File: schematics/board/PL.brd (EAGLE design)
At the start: 89 x 89 mm, 39 parts, among them IC2 STM32F103C8T, Q5 8MHz

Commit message: Папка с платами
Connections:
- net 5V: now also BSK4.3; no longer BSK4.8
- net BUS+: now also BSK4.4; no longer BSK4.7
- net I2CINT: now also BSK4.6; no longer BSK4.3
- net SCLTM: now also BSK4.8; no longer BSK4.5
- net SDATM: now also BSK4.7; no longer BSK4.4
- net TIME: now also BSK4.5; no longer BSK4.2
- net VDD: now also BSK4.2; no longer BSK4.6
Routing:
- net 5V: track 109.7 -> 122.4 mm
- net SDATM: track 38.2 -> 31.7 mm
- net I2CINT: track 29.2 -> 24.5 mm
- net TIME: track 31.1 -> 27.0 mm
- net VDD: track 265.3 -> 267.5 mm
- net NRST: track 49.2 -> 47.8 mm
- net SCLTM: track 32.4 -> 31.8 mm, vias 2 -> 4

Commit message: Обновлен список плат, работа над платой ПН
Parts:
- removed BSK4: (no value), pinheadCS:1X08
- removed C005R: 32,768KHz, CanCubeSat:C005R
- removed C15, C48, C53, C54, C55: 100nF, rcl:C0603
- removed C16: 10µ, rcl:C1206
- removed C44, C45: 27pF, rcl:C0603
- removed C46, C47: 10pF, rcl:C0603
- removed IC2: STM32F103C8T, CanCubeSat:LQFP48
- removed ME-O2: ME-O2, CanCubeSat:ME-O2
- removed MICS-6814: MICS-6814, CanCubeSat:MICS-6814
- removed PB5, PWR: (no value), led:CHIPLED_0603
- removed Q5: 8MHz, 9C-8.000MEEJ-T:XTAL_9C-8.000MEEJ-T
- removed R101, R102: 5k1, resistor:R0603
- removed R64, R79: 10k, resistor:R0603
- removed R78: 1M, resistor:R0603
- removed R81, R82: 2k, resistor:R0603
- removed USB-C: USB-C, CanCubeSat:USB-C
- added 2N6517, BC546: DS1820, CanCubeSat:TO92/TO226
- added BSK1: (no value), pinheadCS:2X05
- added C1, C18, C2, C20, C3, C6: 100nF, rcl:C0603
- added C10: 10nF, rcl:C0603
- added C13, C9: 2,2µ, rcl:C0603
- added C19: 10µ, rcl:C1206
- added C4, C5: 22nF, rcl:C1210
- added C7: 100pF, rcl:C0603
- added C8: 1nF, rcl:C0603
- added COMPR, HEAT, TEMP, VALVE1, VALVE2: (no value), pinheadCS:1X02
- added D1, D2, D3, D4, D5: DIODE-MBR, CanCubeSat:SOD123
- added LED2, LED3: (no value), led:CHIPLED_0603
- added R10, R11, R12, R37, R38, R39, R40, R41, R42, R43, R44, R45: 10k, resistor:R0603
- added R13, R20, R24, R30, R34, R48: 0.05A, rcl:R1210
- added R14, R21, R22, R28, R32, R46, R49, R53, R55: 1M, resistor:R0603
- added R15, R16: 2k, resistor:R0603
- added R17, R18: 5k1, resistor:R0603
- added R19, R23, R29, R31, R33, R47, R50, R54, R56: 100R, resistor:R0603
- added R35: 100k, resistor:R0603
- added R36: 3k3, resistor:R0603
- added R51: 124k, resistor:R0603
- added R52: 22k, resistor:R0603
- added U$1: MS5611, CanCubeSat:MS5611
- added U$10, U$11, U$12, U$13: BA159, CanCubeSat:BA159
- added U$14: ECAP, CanCubeSat:ECAP1MK
- added U$15: DOSIM, CanCubeSat:DOSIM
- added U$16, U$21: FFC-CONNECT68611, CanCubeSat:68611
- added U$17: 33mH, CanCubeSat:RCH114NP
- added U$18, U$19, U$20, U$22, U$23, U$3, U$4, U$5, U$7, U$8: SI2302CDS, CanCubeSat:SOT23-3
- added U$2: Q24, CanCubeSat:Q24
- added U$9: 100µ, CanCubeSat:ECAP100-CMD
- added U1: STM32F405RGT6, STM32F405RGT6:QFP50P1200X1200X160-64N
- added U2: LMC555CMX/NOPB, LMC555CMX_NOPB:SOIC127P599X175-8N
- added VR1: 3362H-1-502LF, CanCubeSat:TRIM_3362H-1-502LF
- R1: value 10k -> 0.5A; device resistor:R0603 -> rcl:R1210
- R2: value 10k -> 1k
- R25: value 5k1 -> 1M
- R26: value 5k1 -> 100R
- R27: value 10k -> 0.05A; device resistor:R0603 -> rcl:R1210
- R3: value 10k -> 4k7
- R4: value 10k -> 22k
- R5, R6, R7, R8, R9: value 10k -> 1M
- moved R1 310.3 mm to (3.00, -247.0), turned to 0 degrees
- moved R26 226.4 mm to (1.50, -193.5), turned to 0 degrees
- moved R25 224.3 mm to (7.50, -193.5), turned to 0 degrees
- moved R27 218.6 mm to (3.00, -187.0), turned to 0 degrees
- moved R3 191.3 mm to (-126.0, 107.0), turned to 0 degrees
- moved R2 123.6 mm to (-57.0, 88.0), turned to 0 degrees
- moved BME280 110.5 mm to (-17.5, -18.5)
- moved R4 55.6 mm to (12.5, 40.0), turned to 0 degrees
- moved R9 54.2 mm to (12.5, 52.5), turned to 0 degrees
- moved R5 51.1 mm to (12.5, 42.5), turned to 0 degrees
- moved R8 50.1 mm to (12.5, 50.0), turned to 0 degrees
- moved R6 46.7 mm to (12.5, 45.0), turned to 0 degrees
- moved R7 46.1 mm to (12.5, 47.5), turned to 0 degrees
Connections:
- removed net I2CINT: BSK4.6, IC2.43
- removed net N$133: C44.1, IC2.6, Q5.1, R78.1
- removed net N$145: C45.1, IC2.5, Q5.2, R78.2
- removed net N$148: C005R.P$2, C47.1, IC2.4
- removed net N$152: C005R.P$1, C46.1, IC2.3
- removed net N$159: PWR.C, R82.2
- removed net N$161: IC2.41, R81.1
- removed net RX-C: IC2.31, USB-C.RX0
- removed net SCLTM: BSK4.8, IC2.45, R25.2
- removed net SDATM: BSK4.7, IC2.46, R26.2
- removed net SENS_CO: IC2.12, MICS-6814.P$5, R3.1
- removed net SENS_CTL_CO_1: IC2.19, R3.2, R6.1
- removed net SENS_CTL_CO_2: IC2.18, R6.2, R7.1
- removed net SENS_CTL_NH3_1: IC2.17, R2.2, R5.1
- removed net SENS_CTL_NH3_2: IC2.16, R5.2, R8.1
- removed net SENS_CTL_NO2_1: IC2.15, R1.2, R4.1
- removed net SENS_CTL_NO2_2: IC2.14, R4.2, R9.1
- removed net SENS_NH3: IC2.11, MICS-6814.P$4, R2.1
- removed net SENS_NO2: IC2.10, MICS-6814.P$3, R1.1
- removed net SENS_O2: IC2.13, ME-O2.P$1
- removed net TX-C: IC2.30, USB-C.TX0
- removed net VDD: BSK4.2, C15.1, C16.1, C48.1, C53.1, C54.1, C55.1, IC2.1, IC2.24, IC2.36, IC2.48, IC2.9, ME-O2.P$7, PB5.A, PWR.A, R101.1, R102.1, R25.1, R26.1, R27.1, R64.1, R7.2, R79.1, R8.2, R9.2, USB-C.3V3/BUS0, USB-C.3V3/BUS1
- new net 3V3: BSK1.3, C10.2, C18.2, C19.2, C2.2, C20.2, C3.2, C6.2, LED2.A, LED3.A, R10.2, R11.2, R12.2, R17.1, R18.1, R43.2, R44.2, R45.2, R52.2, U$2.P$4, U$21.P$1, U$21.P$2, U1.1, U1.13, U1.19, U1.32, U1.48, U1.64
- new net 4OXV: R26.1, U1.9
- new net BME280-EXT: R19.1, U1.35
- new net BME280-INT: R47.1, U1.34
- new net CO: R39.1, U$16.P$7, U1.16
- new net COMPR: R54.1, U1.57
- new net CTRL-CO-1: R39.2, R42.1, U1.27
- new net CTRL-CO-2: R42.2, R43.1, U1.26
- new net CTRL-NH3-1: R38.2, R41.1, U1.45
- new net CTRL-NH3-2: R41.2, R44.1, U1.44
- new net CTRL-NO2-1: R37.2, R40.1, U1.23
- new net CTRL-NO2-2: R40.2, R45.1, U1.22
- new net DOS-G: 2N6517.1, BC546.1, C1.1, C5.2, D1.A, R34.1, R35.2, U$10.P$1, U$14.P$2, U$9.P$1, U2.1
- new net DOSE: BC546.3, C7.2, R36.2
- new net DOSIM: R33.1, U1.10
- new net G-4OXV: R27.1, U$16.P$2
- new net G-BME: R48.1, U$16.P$14
- new net G-MICS: R24.1, U$16.P$6
- new net G-MS: R30.1, U$16.P$11
- new net GND-40XV: U$5.3
- new net GND-4OXV: R27.2
- new net GND-BME-EXT: R20.2, U$3.3
- new net GND-BME-INT: R48.2, U$18.3
- new net GND-COMPR: COMPR.2, U$22.3
- new net GND-DOSIM: R34.2, U$8.3
- new net GND-HEAT: HEAT.2, U$23.3
- new net GND-MICS: R24.2, U$4.3
- new net GND-MS-EXT: R13.2, U$19.3
- new net GND-MS-INT: R30.2, U$7.3
- new net GND-OUT: BSK1.5, BSK1.6, R1.2
- new net GND-VALVE: U$20.3, VALVE1.2, VALVE2.2
- new net HEAT: R56.1, U1.11
- new net MICS: R23.1, U1.8
- new net MS5611-EXT: R31.1, U1.41
- new net MS5611-INT: R29.1, U1.33
- new net N$10: R46.1, R47.2, U$18.1
- new net N$11: R22.1, R31.2, U$19.1
- new net N$12: R28.1, R29.2, U$7.1
- new net N$14: R32.1, R33.2, U$8.1
- new net N$15: C1.2, R2.1, U2.2, U2.6
- new net N$16: R2.2, VR1.2, VR1.3
- new net N$17: R3.2, U2.3, VR1.1
- new net N$18: 2N6517.2, R3.1
- new net N$19: 2N6517.3, C4.1, U$10.P$2, U$11.P$1, U$17.P$2
- new net N$2: R14.1, R19.2, U$3.1
- new net N$20: C5.1, U$11.P$2, U$12.P$1
- new net N$21: C4.2, U$12.P$2, U$13.P$1
- new net N$22: R4.2, R5.2, U$13.P$2, U$14.P$1
- new net N$23: D1.C, D2.A
- new net N$24: D2.C, D3.A
- new net N$25: D3.C, D4.A
- new net N$26: D4.C, D5.A
- new net N$27: D5.C, R4.1
- new net N$28: R5.1, R6.1
- new net N$29: C13.2, U1.47
- new net N$3: BME280.P$2, R20.1
- new net N$30: R6.2, R7.2
- new net N$31: R7.1, R8.1
- new net N$32: R8.2, R9.2
- new net N$33: R9.1, U$15.P$1
- new net N$34: BC546.2, C7.1, R35.1, U$15.P$2
- new net N$36: C9.2, U1.31
- new net N$37: LED2.C, R15.2
- new net N$38: R15.1, U1.53
- new net N$4: C8.2, U$2.P$3
- new net N$40: LED3.C, R16.2
- new net N$47: R53.1, R54.2, U$22.1
- new net N$48: R55.1, R56.2, U$23.1
- new net N$5: C8.1, U1.5
- new net N$6: R21.1, R23.2, U$4.1
- new net N$7: R49.1, R50.2, U$20.1
- new net N$8: R25.1, R26.2, U$5.1
- new net NH3: R38.1, U$16.P$8, U1.15
- new net NO2: R37.1, U$16.P$9, U1.14
- new net RX-O2: U$16.P$4, U1.43
- new net RX-S: U$21.P$5, U1.51
- new net SCL-TM: BSK1.7, U1.29
- new net SDA-TM: BSK1.8, U1.30
- new net TEMP: R51.2, R52.1, TEMP.1, U1.20
- new net TX-O2: U$16.P$3, U1.42
- new net TX-S: U$21.P$7, U1.52
- new net VALVE: R50.1, U1.61
- net 5V: now also BSK1.4, HEAT.1, R36.1, U$1.P$1, U$1.P$7, U$16.P$1, U$16.P$10, U$16.P$15, U$16.P$5, U$17.P$1, U$9.P$2, U2.4, U2.8, VALVE1.1, VALVE2.1; no longer BSK4.3, MICS-6814.P$1
- net BUS+: now also BSK1.2, COMPR.1; no longer BSK4.4
- net GND: now also C10.1, C13.1, C18.1, C19.1, C2.1, C20.1, C3.1, C6.1, C9.1, R1.1, R14.2, R16.1, R21.2, R22.2, R25.2, R28.2, R32.2, R46.2, R49.2, R51.1, R53.2, R55.2, TEMP.2, U$18.2, U$19.2, U$2.P$2, U$20.2, U$21.P$10, U$21.P$4, U$21.P$6, U$21.P$8, U$22.2, U$23.2, U$3.2, U$4.2, U$5.2, U$7.2, U$8.2, U1.12, U1.18, U1.28, U1.60, U1.63; no longer BME280.P$2, BSK4.1, C15.2, C16.2, C44.2, C45.2, C46.2, C47.2, C48.2, C53.2, C54.2, C55.2, IC2.20, IC2.23, IC2.35, IC2.44, IC2.47, IC2.8, ME-O2.P$4, MICS-6814.P$2, R82.1, USB-C.GND0, USB-C.GND1
- net N$1: now also R13.1, U$1.P$3, U$1.P$6; no longer PB5.C, R81.2
- net NRST: now also R10.1, U$21.P$3, U1.7; no longer IC2.7, R79.2, USB-C.NRST/EN
- net SCL: now also R17.2, U$1.P$5, U$16.P$12, U1.58; no longer IC2.21, R101.2
- net SDA: now also R18.2, U$1.P$4, U$16.P$13, U1.59; no longer IC2.22, R102.2
- net SWC: now also R12.1, U$21.P$11, U1.49; no longer IC2.37, R27.2, USB-C.SWC/TXD
- net SWD: now also R11.1, U$21.P$9, U1.46; no longer IC2.34, R64.2, USB-C.SWD/RXD
- net TIME: now also BSK1.9, U1.50; no longer BSK4.5, IC2.42
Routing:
- net VDD: track 267.5 -> 0.00 mm, vias 13 -> 0
- net 5V: track 122.4 -> 0.00 mm
- net NRST: track 47.8 -> 0.00 mm, vias 2 -> 0
- net GND: track 40.0 -> 0.00 mm, vias 3 -> 0
- net SENS_CO: track 36.7 -> 0.00 mm, vias 1 -> 0
- net SENS_NH3: track 36.7 -> 0.00 mm, vias 1 -> 0
- net SENS_NO2: track 34.2 -> 0.00 mm, vias 2 -> 0
- net TX-C: track 34.0 -> 0.00 mm, vias 2 -> 0
- net SDA: track 32.3 -> 0.00 mm, vias 1 -> 0
- net SCLTM: track 31.8 -> 0.00 mm, vias 4 -> 0
- net SDATM: track 31.7 -> 0.00 mm
- net SENS_O2: track 30.6 -> 0.00 mm, vias 4 -> 0
- net RX-C: track 29.7 -> 0.00 mm, vias 2 -> 0
- net SWD: track 29.4 -> 0.00 mm, vias 2 -> 0
- net SCL: track 27.9 -> 0.00 mm, vias 1 -> 0
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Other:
- board size 89 x 89 mm -> 82 x 92 mm

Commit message: Схема БКУ
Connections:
- net GND: no longer U$21.P$10, U$21.P$4, U$21.P$6, U$21.P$8
- net GND-OUT: now also U$21.P$10, U$21.P$4, U$21.P$6, U$21.P$8
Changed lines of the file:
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@@
 <contactref element="TEMP" pad="2"/>
 <contactref element="R51" pad="1"/>
-<contactref element="U$21" pad="P$8"/>
-<contactref element="U$21" pad="P$4"/>
-<contactref element="U$21" pad="P$6"/>
-<contactref element="U$21" pad="P$10"/>
 <wire x1="4.95" y1="-233.5" x2="1.6" y2="-247" width="0" layer="19" extent="1-1"/>
 <wire x1="8.35" y1="-228.5" x2="4.95" y2="-233.5" width="0" layer="19" extent="1-1"/>
@@
 <wire x1="8.35" y1="-136" x2="2.35" y2="-146" width="0" layer="19" extent="1-1"/>
 <wire x1="10.45" y1="-129" x2="8.35" y2="-136" width="0" layer="19" extent="1-1"/>
+<wire x1="42.85" y1="-238.5" x2="8.35" y2="-228.5" width="0" layer="19" extent="1-1"/>
+<wire x1="45.45" y1="-228.5" x2="42.85" y2="-238.5" width="0" layer="19" extent="1-1"/>
 <wire x1="20.65" y1="-90" x2="10.45" y2="-129" width="0" layer="19" extent="1-1"/>
 <wire x1="25.65" y1="-85" x2="20.65" y2="-90" width="0" layer="19" extent="1-1"/>
@@
 <wire x1="37.825" y1="-91.85" x2="36.15" y2="-85" width="0" layer="19" extent="1-1"/>
 <wire x1="11.1" y1="-78.5" x2="23.15" y2="-78" width="0" layer="19" extent="1-1"/>
-<wire x1="58.25" y1="29.67" x2="11.1" y2="-78.5" width="0" layer="19" extent="1-1"/>
-<wire x1="63.25" y1="29.67" x2="58.25" y2="29.67" width="0" layer="19" extent="1-1"/>
-<wire x1="65.67" y1="25.75" x2="63.25" y2="29.67" width="0" layer="19" extent="1-1"/>
-<wire x1="63.25" y1="18.33" x2="65.67" y2="25.75" width="0" layer="19" extent="1-1"/>
-<wire x1="61.75" y1="18.33" x2="63.25" y2="18.33" width="0" layer="19" extent="1-1"/>
 <wire x1="0.65" y1="-85" x2="11.1" y2="-78.5" width="0" layer="19" extent="1-1"/>
-<wire x1="45.45" y1="-228.5" x2="1.6" y2="-247" width="0" layer="19" extent="1-1"/>
-<wire x1="42.85" y1="-238.5" x2="45.45" y2="-228.5" width="0" layer="19" extent="1-1"/>
-<wire x1="59.27" y1="89.8" x2="42.85" y2="-238.5" width="0" layer="19" extent="1-1"/>
-<wire x1="45.45" y1="-298" x2="59.27" y2="89.8" width="0" layer="19" extent="1-1"/>
+<wire x1="45.45" y1="-298" x2="42.85" y2="-238.5" width="0" layer="19" extent="1-1"/>
 <wire x1="42.85" y1="-308" x2="45.45" y2="-298" width="0" layer="19" extent="1-1"/>
 <wire x1="45.45" y1="-330" x2="42.85" y2="-308" width="0" layer="19" extent="1-1"/>
@@
 <wire x1="42.85" y1="-356" x2="45.45" y2="-346" width="0" layer="19" extent="1-1"/>
 <wire x1="41.15" y1="-361" x2="42.85" y2="-356" width="0" layer="19" extent="1-1"/>
-<wire x1="56" y1="6.65" x2="41.15" y2="-361" width="0" layer="19" extent="1-1"/>
-<wire x1="58" y1="6.65" x2="56" y2="6.65" width="0" layer="19" extent="1-1"/>
-<wire x1="60" y1="6.65" x2="58" y2="6.65" width="0" layer="19" extent="1-1"/>
-<wire x1="62" y1="6.65" x2="60" y2="6.65" width="0" layer="19" extent="1-1"/>
+<wire x1="61.75" y1="18.33" x2="42.65" y2="-78" width="0" layer="19" extent="1-1"/>
+<wire x1="63.25" y1="18.33" x2="61.75" y2="18.33" width="0" layer="19" extent="1-1"/>
+<wire x1="65.67" y1="25.75" x2="63.25" y2="18.33" width="0" layer="19" extent="1-1"/>
+<wire x1="63.25" y1="29.67" x2="65.67" y2="25.75" width="0" layer="19" extent="1-1"/>
+<wire x1="58.25" y1="29.67" x2="63.25" y2="29.67" width="0" layer="19" extent="1-1"/>
+<wire x1="59.27" y1="89.8" x2="58.25" y2="29.67" width="0" layer="19" extent="1-1"/>
 </signal>
 <signal name="SCL">
@@
 <contactref element="BSK1" pad="6"/>
 <contactref element="BSK1" pad="5"/>
-<wire x1="42.27" y1="83.64" x2="4.4" y2="-247" width="0" layer="19" extent="1-1"/>
-<wire x1="42.27" y1="81.1" x2="42.27" y2="83.64" width="0" layer="19" extent="1-1"/>
+<contactref element="U$21" pad="P$10"/>
+<contactref element="U$21" pad="P$8"/>
+<contactref element="U$21" pad="P$6"/>
+<contactref element="U$21" pad="P$4"/>
+<wire x1="56" y1="6.65" x2="4.4" y2="-247" width="0" layer="19" extent="1-1"/>
+<wire x1="58" y1="6.65" x2="56" y2="6.65" width="0" layer="19" extent="1-1"/>
+<wire x1="60" y1="6.65" x2="58" y2="6.65" width="0" layer="19" extent="1-1"/>
+<wire x1="62" y1="6.65" x2="60" y2="6.65" width="0" layer="19" extent="1-1"/>
+<wire x1="42.27" y1="81.1" x2="56" y2="6.65" width="0" layer="19" extent="1-1"/>
+<wire x1="42.27" y1="83.64" x2="42.27" y2="81.1" width="0" layer="19" extent="1-1"/>
 </signal>
 <signal name="N$15">

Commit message: Плата ПН почти разведена. Осталось добавить конденсаторы на компрессор и клапаны и запитать AVCC МК через стабилизатор напряжения
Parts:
- BME280: value BME280 -> BME280BME280-PINS-ONLY; device CanCubeSat:BME280 -> CanCubeSat:BME280-PINS-ONLY
- U$1: value MS5611 -> MS5611MS5611-PIN-ONLY; device CanCubeSat:MS5611 -> CanCubeSat:MS5611-PINS-ONLY
- moved R52 409.8 mm to (58.0, 43.5)
- moved R51 407.0 mm to (58.0, 45.7), turned to 180 degrees
- moved R55 402.2 mm to (61.5, 45.7)
- moved R56 395.0 mm to (61.5, 43.5), turned to 180 degrees
- moved U$23 393.9 mm to (61.5, 48.5)
- moved R53 349.6 mm to (31.8, 9.50), turned to 90 degrees
- moved R54 344.6 mm to (34.0, 9.50), turned to 270 degrees
- moved U$22 338.9 mm to (29.0, 9.50), turned to 90 degrees
- moved R49 314.2 mm to (31.8, 6.00), turned to 90 degrees
- moved R50 309.1 mm to (34.0, 6.00), turned to 270 degrees
- moved U$20 303.4 mm to (29.0, 6.00), turned to 90 degrees
- moved U$8 285.5 mm to (54.5, 48.5)
- moved R34 279.8 mm to (54.5, 53.0), turned to 270 degrees
- moved R32 278.2 mm to (54.5, 45.7)
- moved R48 277.7 mm to (24.5, 32.0)
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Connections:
- removed net GND-40XV: U$5.3
- removed net RX-O2: U$16.P$4, U1.43
- removed net SCL: BME280.P$3, R17.2, U$1.P$5, U$16.P$12, U1.58
- removed net SDA: BME280.P$4, R18.2, U$1.P$4, U$16.P$13, U1.59
- removed net TX-O2: U$16.P$3, U1.42
- new net O2: U$16.P$3, U1.17
- new net SENS-EXT-SCL: BME280.P$3, U$1.P$5, U1.41
- new net SENS-EXT-SDA: BME280.P$4, U$1.P$4, U1.40
- new net SENS-INT-SCL: R17.2, U$16.P$12, U1.58
- new net SENS-INT-SDA: R18.2, U$16.P$13, U1.59
- net 4OXV: now also U1.45; no longer U1.9
- net BME280-EXT: now also U1.8; no longer U1.35
- net BME280-INT: now also U1.27; no longer U1.34
- net CTRL-CO-1: now also U1.35; no longer U1.27
- net CTRL-CO-2: now also U1.42; no longer U1.26
- net CTRL-NH3-1: now also U1.33; no longer U1.45
- net CTRL-NH3-2: now also U1.34; no longer U1.44
- net DOSE: now also U1.54
- net GND-4OXV: now also U$5.3
- net GND-OUT: now also U$21.P$3, U$21.P$5, U$21.P$7, U$21.P$9; no longer U$21.P$10, U$21.P$4, U$21.P$6, U$21.P$8
- net MICS: now also U1.44; no longer U1.8
- net MS5611-EXT: now also U1.9; no longer U1.41
- net MS5611-INT: now also U1.26; no longer U1.33
- net NRST: now also U$21.P$11; no longer U$21.P$3
- net RX-S: now also U$21.P$4; no longer U$21.P$5
- net SWC: now also U$21.P$10; no longer U$21.P$11
- net SWD: now also U$21.P$8; no longer U$21.P$9
- net TX-S: now also U$21.P$6; no longer U$21.P$7
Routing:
- net GND-OUT: track 0.00 -> 299.1 mm, vias 0 -> 3
- net GND: track 0.00 -> 284.7 mm, vias 0 -> 15
- net 5V: track 0.00 -> 250.3 mm, vias 0 -> 2
- net 3V3: track 0.00 -> 200.4 mm, vias 0 -> 13
- net BUS+: track 0.00 -> 124.7 mm
- net DOS-G: track 0.00 -> 103.9 mm
- net DOSE: track 0.00 -> 98.6 mm, vias 0 -> 2
- net TIME: track 0.00 -> 68.1 mm, vias 0 -> 3
- net O2: track 0.00 -> 64.9 mm, vias 0 -> 2
- net SENS-INT-SDA: track 0.00 -> 62.8 mm
- net SENS-EXT-SDA: track 0.00 -> 61.3 mm, vias 0 -> 1
- net SENS-INT-SCL: track 0.00 -> 61.1 mm
- net CO: track 0.00 -> 56.4 mm, vias 0 -> 2
- net NO2: track 0.00 -> 56.1 mm, vias 0 -> 2
- net TEMP: track 0.00 -> 55.4 mm
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
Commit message: Плата ПН готова к проверке
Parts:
- added C11, C12: 1uF, CanCubeSat:ECAP-SMD-D4
- added U$24, U$6: 220uF, CanCubeSat:ECAP220-CMD
- added U$25: ADP150AUJZ-3.3-R7, CanCubeSat:SOT23-5
- U$14: value ECAP -> 1uF
- turned C3 to 270 degrees
- renumbered U$1 to MS5611
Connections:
- new net N$9: C11.P+, C3.1, U$25.P$5, U1.13
- net 3V3: no longer C3.2, U1.13
- net 5V: now also C12.P+, U$24.P$1, U$25.P$1, U$25.P$3
- net BUS+: now also U$6.P$1
- net GND: now also C11.P-, C12.P-, C3.2, U$25.P$2; no longer C3.1
- net GND-COMPR: now also U$6.P$2
- net GND-VALVE: now also U$24.P$2
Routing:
- net GND: track 284.7 -> 333.4 mm, vias 15 -> 16
- net 5V: track 250.3 -> 290.7 mm
- net N$9: track 0.00 -> 15.5 mm, vias 0 -> 2
- net NRST: track 38.8 -> 30.5 mm
- net BUS+: track 124.7 -> 131.7 mm
- net GND-VALVE: track 17.1 -> 22.3 mm
- net DOS-G: track 103.9 -> 99.3 mm, vias 0 -> 2
- net GND-COMPR: track 9.67 -> 12.8 mm
- net 3V3: track 200.4 -> 202.7 mm
- net N$1: track 13.2 -> 11.5 mm
- net SENS-EXT-SCL: track 53.6 -> 55.1 mm
- net NO2: track 56.1 -> 54.7 mm
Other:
- board text added: "PC12"
- board text added: "PWR"
- board text added: "for firmware"
- board text added: "to BSK1"
- board text added: "to Sealed housing"

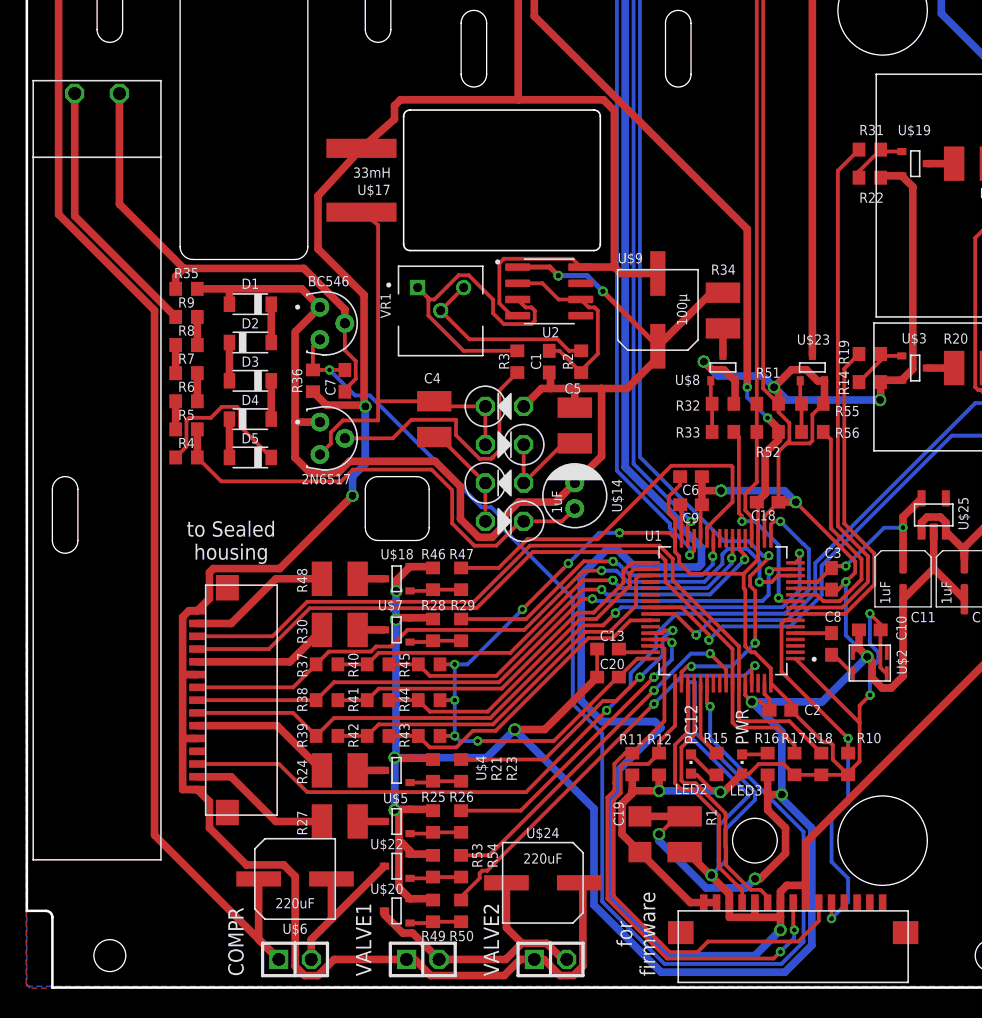
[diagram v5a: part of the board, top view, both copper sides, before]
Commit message: Добавил красоты на плате ПН, поправил подтяжки некоторых транзисторов
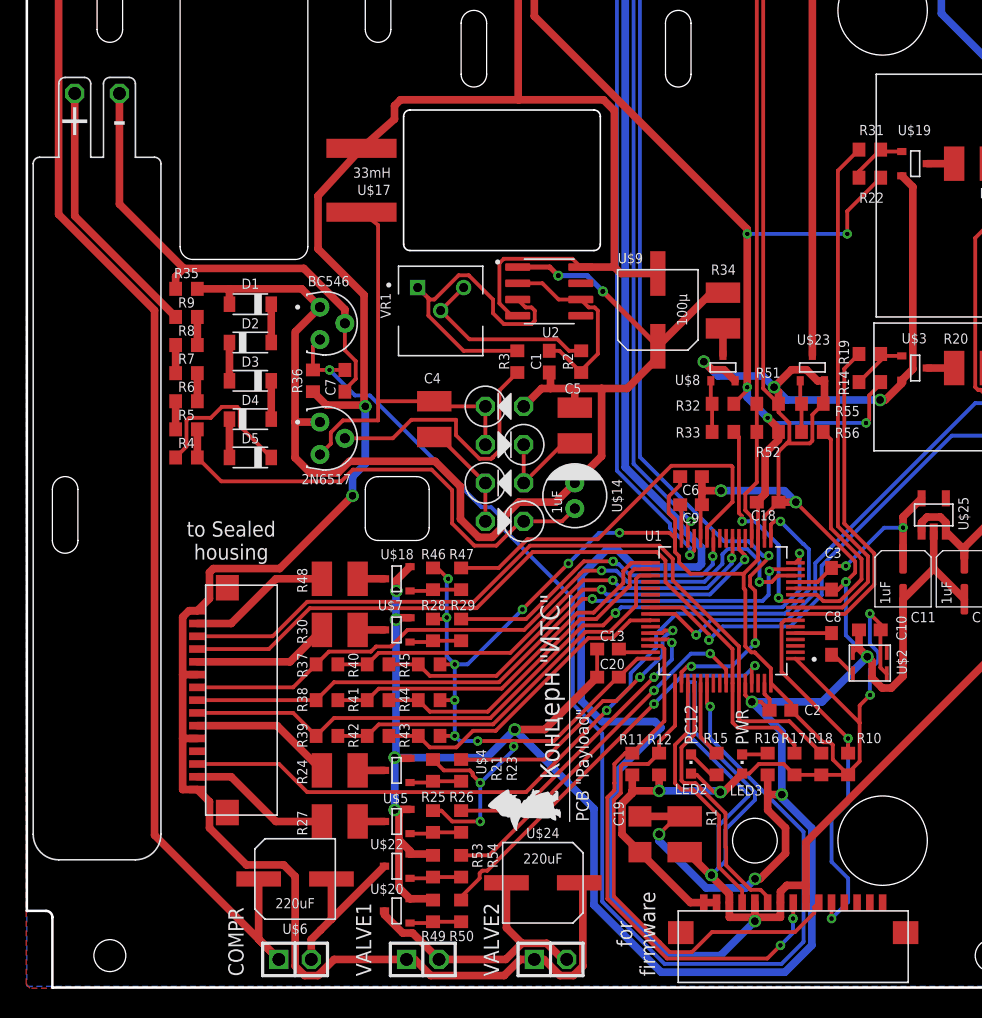
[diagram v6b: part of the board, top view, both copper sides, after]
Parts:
- added U$1, U$26: PCB "Payload", CanCubeSat:ITS-LOGO
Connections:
- net 3V3: now also R14.2, R21.2, R22.2, R25.2, R28.2, R32.2, R46.2
- net GND: no longer R14.2, R21.2, R22.2, R25.2, R28.2, R32.2, R46.2
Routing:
- net 3V3: track 202.7 -> 255.0 mm, vias 13 -> 21
- net GND: track 333.4 -> 321.9 mm
- net GND-OUT: track 299.1 -> 296.6 mm
- net SWC: track 40.1 -> 39.5 mm

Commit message: Двигаем логотип на плате ПН
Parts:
- moved U$26 28.9 mm to (43.0, 7.00)
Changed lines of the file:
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@@
 <layer number="25" name="tNames" color="7" fill="1" visible="yes" active="yes"/>
 <layer number="26" name="bNames" color="7" fill="1" visible="yes" active="yes"/>
-<layer number="27" name="tValues" color="7" fill="1" visible="no" active="yes"/>
+<layer number="27" name="tValues" color="7" fill="1" visible="yes" active="yes"/>
 <layer number="28" name="bValues" color="7" fill="1" visible="no" active="yes"/>
 <layer number="29" name="tStop" color="7" fill="3" visible="yes" active="yes"/>
@@
 <attribute name="VALUE" x="72.4" y="30" size="0.8" layer="21" ratio="15" rot="R90"/>
 </element>
-<element name="U$1" library="CanCubeSat" package="ITS-LOGO" value="PCB &quot;Payload&quot;" x="42.5" y="13" smashed="yes" rot="R90">
-<attribute name="VALUE" x="44" y="13" size="1" layer="21" font="vector" ratio="15" rot="R90"/>
-</element>
-<element name="U$26" library="CanCubeSat" package="ITS-LOGO" value="PCB &quot;Payload&quot;" x="71.5" y="2" smashed="yes" rot="MR0">
-<attribute name="VALUE" x="71.5" y="0.5" size="1" layer="22" font="vector" ratio="15" rot="MR0"/>
+<element name="U$1" library="CanCubeSat" package="ITS-LOGO" value="PCB &quot;Payload&quot;" x="42.5" y="13" smashed="yes" rot="SR90">
+<attribute name="VALUE" x="44" y="13" size="1" layer="21" font="vector" ratio="15" rot="SR90"/>
+</element>
+<element name="U$26" library="CanCubeSat" package="ITS-LOGO" value="PCB &quot;Payload&quot;" x="43" y="7" smashed="yes" rot="MR0">
+<attribute name="VALUE" x="43" y="5.5" size="1" layer="22" font="vector" ratio="15" rot="MR0"/>
 </element>
 </elements>
